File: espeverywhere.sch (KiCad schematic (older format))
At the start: 37 parts, among them P1 USB_OTG, P3 CONN_01X06, SW2 GPIO0, SW3 RESET, U1 AP2112K-3.3V, U2 ESP-12E, U3 FT230XS

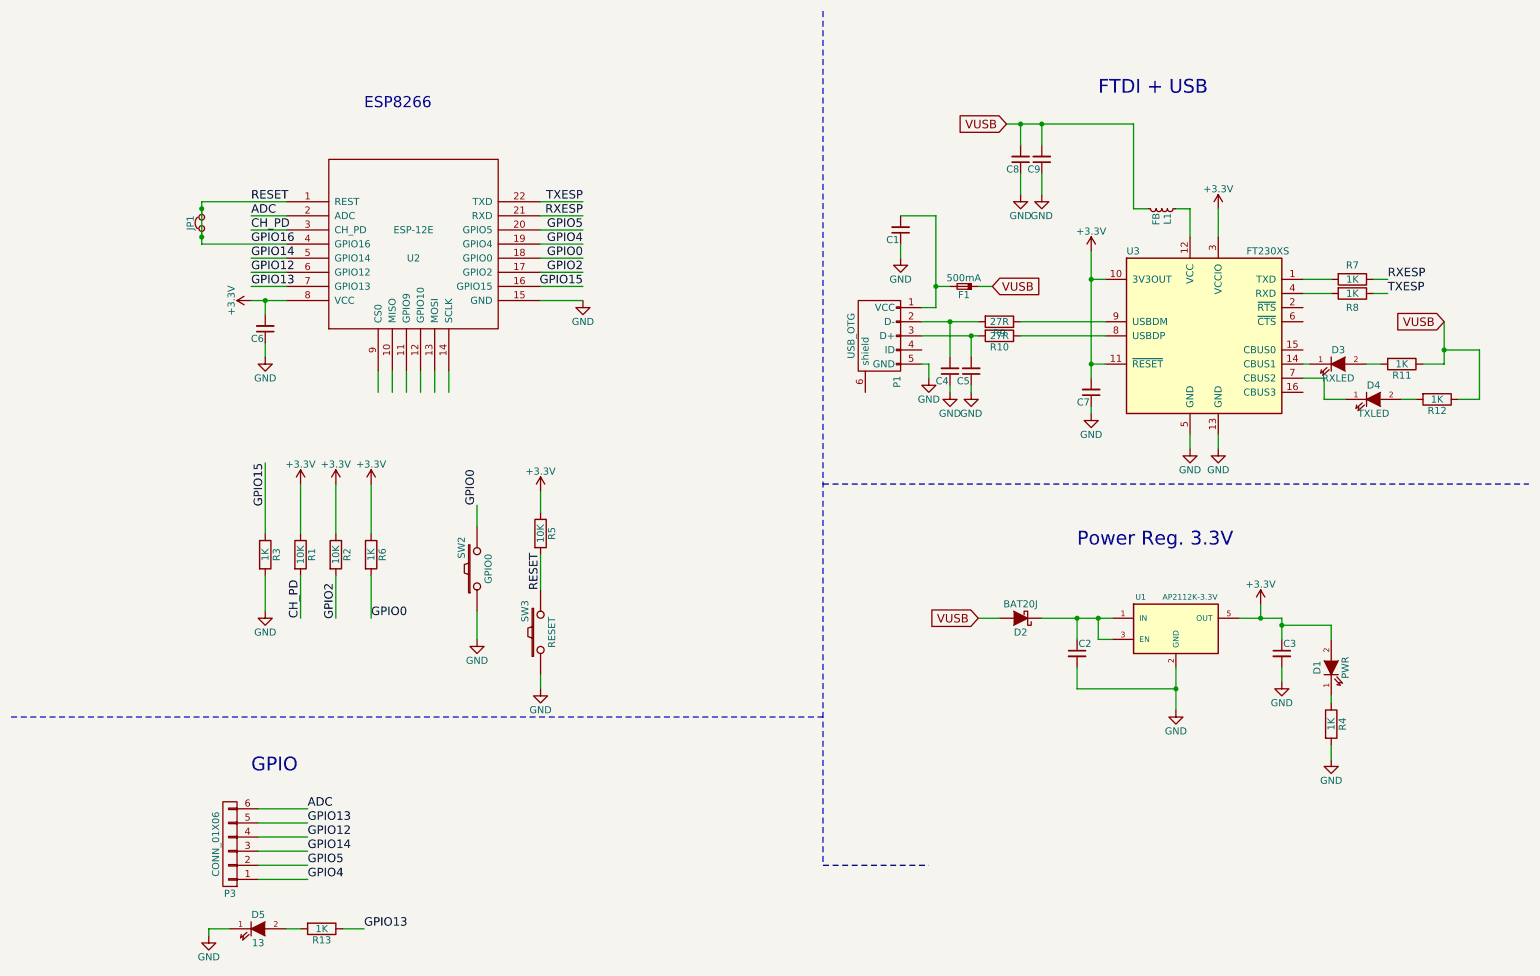
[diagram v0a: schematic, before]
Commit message: Changed JST-SH-6 to 8 Pin
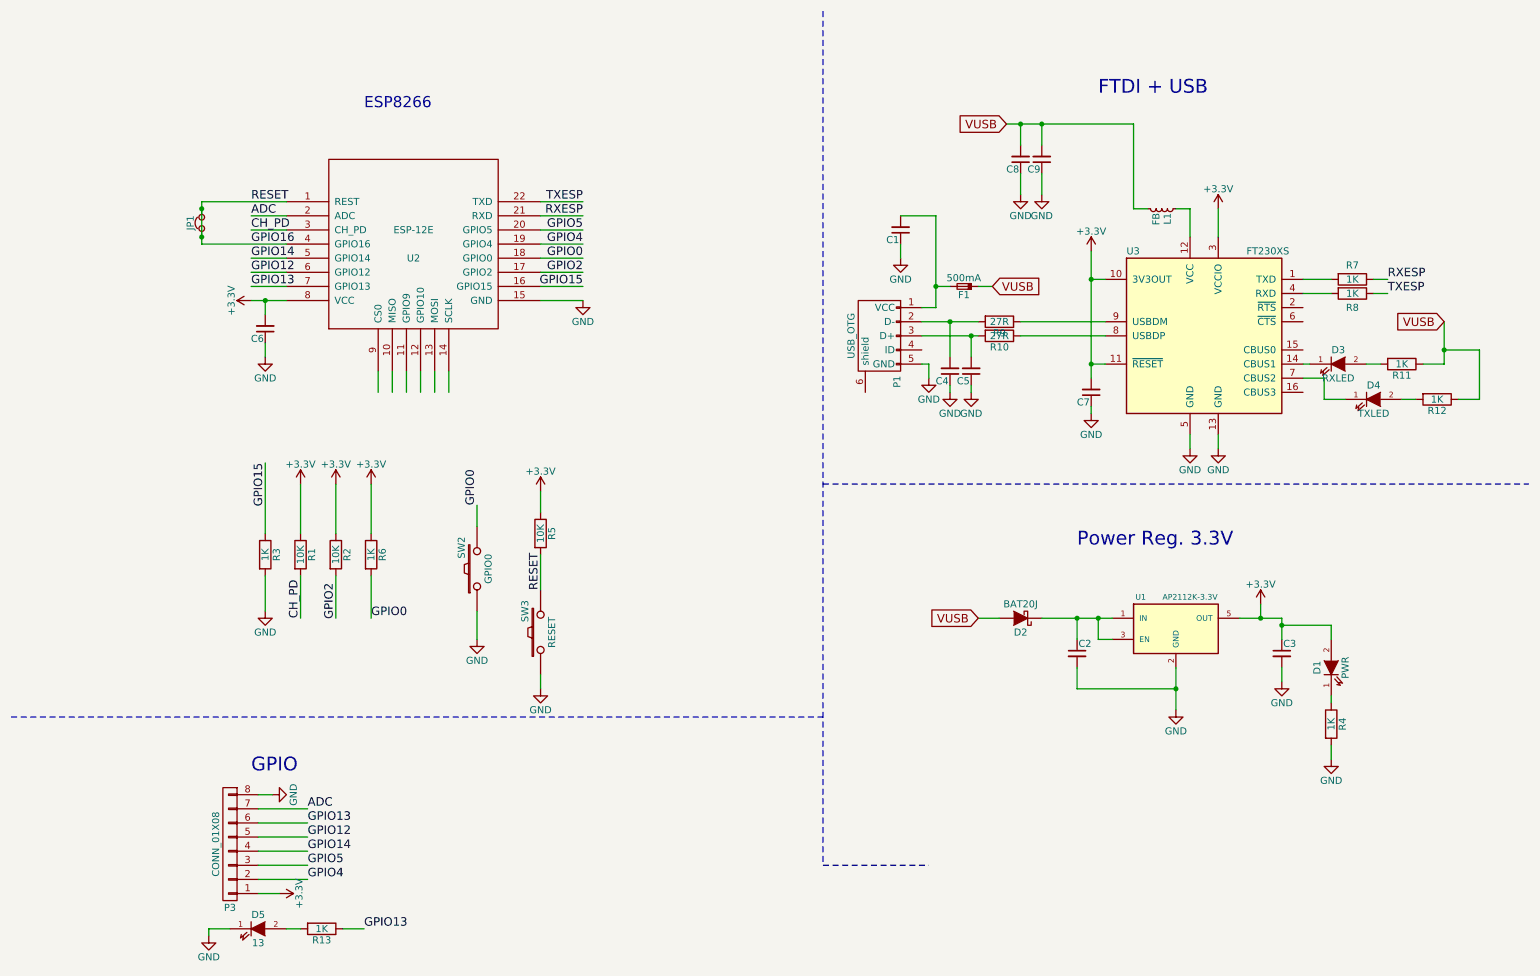
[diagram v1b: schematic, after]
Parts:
- removed P3: CONN_01X06, Connectors_JST_SH:Connectors_JST_SM06B-SRSS-TB, symbol CONN_01X06
- added P3: CONN_01X08, Connectors_JST_SH:Connectors_JST_SM08B-SRSS-TB, symbol CONN_01X08
- C6, C9: footprint project_footprints:C_0402_Hand -> Capacitors_SMD:C_0805
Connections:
- wire segments 127 -> 113
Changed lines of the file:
@@
 Text Label 2500 4800 1    60   ~ 0
 CH_PD
-$Comp
-L CONN_01X06 P3
-U 1 1 5843EDFF
-P 2000 6400
-F 0 "P3" H 2000 6750 50  0000 C CNN
-F 1 "CONN_01X06" V 2100 6400 50  0000 C CNN
-F 2 "Connectors_JST_SH:Connectors_JST_SM06B-SRSS-TB" H 2000 6400 50  0001 C CNN
-F 3 "" H 2000 6400 50  0000 C CNN
-F 4 "455-1806-1-ND" H 2000 6400 60  0001 C CNN "Digikey Part No."
-	1    2000 6400
-	-1   0    0    1
-$EndComp
 Text Label 2150 1850 0    60   ~ 0
 RESET
@@
 F 0 "C6" H 2260 2820 50  0000 L CNN
 F 1 "10uF" H 2260 2670 50  0001 L CNN
-F 2 "project_footprints:C_0402_Hand" H 2250 2750 60  0001 C CNN
+F 2 "Capacitors_SMD:C_0805" H 2250 2750 60  0001 C CNN
 F 3 "" H 2250 2750 60  0000 C CNN
 F 4 "490-1718-1-ND" H 2250 2750 60  0001 C CNN "Digikey Part No."
@@
 F 0 "C9" H 7760 1620 50  0000 L CNN
 F 1 "10uF" H 7760 1470 50  0001 L CNN
-F 2 "project_footprints:C_0402_Hand" H 7750 1550 60  0001 C CNN
+F 2 "Capacitors_SMD:C_0805" H 7750 1550 60  0001 C CNN
 F 3 "" H 7750 1550 60  0000 C CNN
 F 4 "490-1718-1-ND" H 7750 1550 60  0001 C CNN "Digikey Part No."
@@
 F 0 "P1" H 6925 2675 50  0000 C CNN
 F 1 "USB_OTG" H 6600 3000 50  0000 C CNN
-F 2 "" V 6550 2700 50  0000 C CNN
+F 2 "" V 6550 2700 50  0001 C CNN
 F 3 "" V 6550 2700 50  0000 C CNN
 F 4 "609-4618-1-ND" H 6600 2800 60  0001 C CNN "Digikey Part No."
@@
 	2400 2450 2150 2450
 Wire Wire Line
-	2150 2550 2250 2550
-Wire Wire Line
-	2250 2550 2400 2550
+	2150 2550 2400 2550
 Wire Wire Line
 	4200 2550 4500 2550
@@
 Connection ~ 2250 2550
 Wire Wire Line
-	1800 1850 1800 1900
-Wire Wire Line
-	1800 1900 1800 2100
-Wire Wire Line
-	1800 2100 1800 2150
+	1800 1850 1800 2150
 Wire Wire Line
 	3000 4800 3000 4500
@@
 Connection ~ 1800 2100
 Wire Wire Line
-	7750 4800 8000 4800
-Wire Wire Line
-	8000 4800 8150 4800
-Wire Wire Line
-	8150 4800 8250 4800
+	7750 4800 8250 4800
 Wire Wire Line
 	8250 4950 8150 4950
@@
 Connection ~ 8000 4800
 Wire Wire Line
-	8700 5150 8700 5300
-Wire Wire Line
-	8700 5300 8700 5450
+	8700 5150 8700 5450
 Wire Wire Line
 	8000 5150 8000 5300
@@
 Connection ~ 8700 5300
 Wire Wire Line
-	9150 4800 9300 4800
-Wire Wire Line
-	9300 4800 9450 4800
-Wire Wire Line
-	9450 4800 9450 4850
-Wire Wire Line
-	9450 4850 9450 4950
+	9150 4800 9450 4800
+Wire Wire Line
+	9450 4800 9450 4950
 Wire Wire Line
 	9450 5250 9450 5150
@@
 	7000 2600 6900 2600
 Wire Wire Line
-	7000 1950 7000 2450
-Wire Wire Line
-	7000 2450 7000 2600
+	7000 1950 7000 2600
 Wire Wire Line
 	7000 2450 7100 2450
@@
 	7300 2450 7400 2450
 Wire Wire Line
-	6900 2700 7100 2700
-Wire Wire Line
-	7100 2700 7300 2700
+	6900 2700 7300 2700
 Wire Wire Line
 	7600 2700 8200 2700
 Wire Wire Line
-	6900 2800 7250 2800
-Wire Wire Line
-	7250 2800 7300 2800
+	6900 2800 7300 2800
 Wire Wire Line
 	7600 2800 8200 2800
@@
 	8200 2400 8100 2400
 Wire Wire Line
-	8100 2200 8100 2400
-Wire Wire Line
-	8100 2400 8100 3000
-Wire Wire Line
-	8100 3000 8100 3100
+	8100 2200 8100 3100
 Wire Wire Line
 	8800 2100 8800 1900
@@
 	8500 1900 8400 1900
 Wire Wire Line
-	7500 1300 7600 1300
-Wire Wire Line
-	7600 1300 7750 1300
-Wire Wire Line
-	7750 1300 8400 1300
+	7500 1300 8400 1300
 Wire Wire Line
 	8400 1300 8400 1900
@@
 	10600 3000 10450 3000
 Wire Wire Line
-	10600 2700 10600 2900
-Wire Wire Line
-	10600 2900 10600 3000
+	10600 2700 10600 3000
 Wire Wire Line
 	10300 3250 10400 3250
@@
 Wire Notes Line
 	450  5500 6200 5500
+$Comp
+L CONN_01X08 P3
+U 1 1 58923400
+P 2000 6400
+F 0 "P3" H 2000 6850 50  0000 C CNN
+F 1 "CONN_01X08" V 2100 6400 50  0000 C CNN
+F 2 "Connectors_JST_SH:Connectors_JST_SM08B-SRSS-TB" H 2000 6400 50  0001 C CNN
+F 3 "" H 2000 6400 50  0000 C CNN
+F 4 "455-1808-1-ND" H 2000 6400 60  0001 C CNN "Digikey Part No."
+	1    2000 6400
+	-1   0    0    1
+$EndComp
+$Comp
+L GND #PWR027
+U 1 1 58924F6C
+P 2300 6050
+F 0 "#PWR027" H 2300 5800 50  0001 C CNN
+F 1 "GND" H 2300 5900 50  0000 C CNN
+F 2 "" H 2300 6050 60  0000 C CNN
+F 3 "" H 2300 6050 60  0000 C CNN
+	1    2300 6050
+	0    -1   -1   0
+$EndComp
+$Comp
+L +3.3V #PWR028
+U 1 1 58925461
+P 2350 6750
+F 0 "#PWR028" H 2350 6600 50  0001 C CNN
+F 1 "+3.3V" H 2350 6890 50  0000 C CNN
+F 2 "" H 2350 6750 60  0000 C CNN
+F 3 "" H 2350 6750 60  0000 C CNN
+	1    2350 6750
+	0    1    1    0
+$EndComp
+Wire Wire Line
+	2200 6050 2300 6050
+Wire Wire Line
+	2200 6750 2350 6750
 $EndSCHEMATC

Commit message: Breakout Board added
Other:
- note added: "*Works with Cable: 455-3016-ND"
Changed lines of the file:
@@
 Wire Wire Line
 	2200 6750 2350 6750
+Text Notes 2900 6000 0    98   ~ 0
+*Works with Cable:  455-3016-ND
 $EndSCHEMATC
